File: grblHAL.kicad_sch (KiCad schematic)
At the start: 49 parts, among them J1 Conn_01x03, J2 Conn_02x08_Odd_Even, J3 Conn_01x06, J4 Conn_01x06, J5 Conn_01x04, U1 YAAJ_BluePill_Part_Like_SWD_B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, U10 PC817, U11 PC817, U12 PC817, U13 PC817, U14 LM1117-3.3, U2 TMC2208_SILENTSTEPSTICK, U3 buck2596, U4 PC817, U5 PC817, U6 PC817, U7 PC817, U8 PC817, U9 PC817

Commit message: Schematic Layout Nets Opto 4 TMC Stage 2
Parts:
- added C3, C4: 100uF/35v, Capacitor_THT:CP_Radial_D8.0mm_P3.50mm, symbol Device:C_Polarized_Small
- added J6, J7, J8: Conn_01x04, Connector_PinHeader_2.54mm:PinHeader_1x04_P2.54mm_Vertical, symbol Connector_Generic:Conn_01x04
- added U15, U16, U17: TMC2208, TMC2208_SILENTSTEPSTICK:MODULE_TMC2208_SILENTSTEPSTICK, symbol TMC2208_SILENTSTEPSTICK:TMC2208_SILENTSTEPSTICK
- J2: value Conn_02x08_Odd_Even -> Conn
- J3, J4: footprint Connector_Phoenix_MC_HighVoltage:PhoenixContact_MC_1,5_6-G-5.08_1x06_P5.08mm_Horizontal -> Connector_Phoenix_MSTB:PhoenixContact_MSTBA_2,5_6-G-5,08_1x06_P5.08mm_Horizontal
- U2: value TMC2208_SILENTSTEPSTICK -> TMC2208
- U3: footprint Buck2596:buck2596 -> DC_DC_LM2596_small:DC_DC_LM2596_small
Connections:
- net EN is gone; now on net STEN: JP1.2 (B), U2.JP1_8 (EN)
- net 3V3: now also U15.JP2_7 (VIO), U16.JP2_7 (VIO), U17.JP2_7 (VIO)
- net 5V: now also U1.18 (5V); no longer C1.2, C2.2, JP1.1 (A), R12.1, R13.1, U1.19 (GND), U1.39 (GND), U10.3, U11.3, U12.3, U13.3, U14.1 (GND), U2.JP2_2 (GND), U2.JP2_8 (GND), U3.4 (out-), U4.3, U5.3, U6.3, U7.3, U8.3, U9.3
- net DIRX: now also U17.JP1_1 (DIR)
- net DIRY: now also U16.JP1_1 (DIR)
- net DIRZ: now also U15.JP1_1 (DIR)
- net STEN: now also U15.JP1_8 (EN), U16.JP1_8 (EN), U17.JP1_8 (EN)
- net STEPX: now also U17.JP1_2 (STEP)
- net STEPY: now also U16.JP1_2 (STEP)
- net STEPZ: now also U15.JP1_2 (STEP)
- net VM: now also C3.1, C4.1, U15.JP2_1 (VM), U16.JP2_1 (VM), U17.JP2_1 (VM)
- new net: J6.1 (Pin_1), U15.JP2_3 (OA2)
- new net: J6.2 (Pin_2), U15.JP2_4 (OA1)
- new net: J6.3 (Pin_3), U15.JP2_5 (OB1)
- new net: J6.4 (Pin_4), U15.JP2_6 (OB2)
- new net: J7.1 (Pin_1), U16.JP2_3 (OA2)
- new net: J7.2 (Pin_2), U16.JP2_4 (OA1)
- new net: J7.3 (Pin_3), U16.JP2_5 (OB1)
- new net: J7.4 (Pin_4), U16.JP2_6 (OB2)
- new net: J8.1 (Pin_1), U17.JP2_3 (OA2)
- new net: J8.2 (Pin_2), U17.JP2_4 (OA1)
- new net: J8.3 (Pin_3), U17.JP2_5 (OB1)
- new net: J8.4 (Pin_4), U17.JP2_6 (OB2)
- new net GND: C1.2, C2.2, C3.2, C4.2, JP1.1 (A), R12.1, R13.1, U1.19 (GND), U1.39 (GND), U10.3, U11.3, U12.3, U13.3, U14.1 (GND), U15.JP2_2 (GND), U15.JP2_8 (GND), U16.JP2_2 (GND), U16.JP2_8 (GND), U17.JP2_2 (GND), U17.JP2_8 (GND), U2.JP2_2 (GND), U2.JP2_8 (GND), U3.4 (out-), U4.3, U5.3, U6.3, U7.3, U8.3, U9.3
- new net UART1_PDN2: U15.JP1_4 (PDN/UART1)
- new net UART1_PDN3: U16.JP1_4 (PDN/UART1)
- new net UART1_PDN4: U17.JP1_4 (PDN/UART1)
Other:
- moved on the sheet: C1, C2, D1, D10, D11, D12, D13, D2, D3, D4, D5, D6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

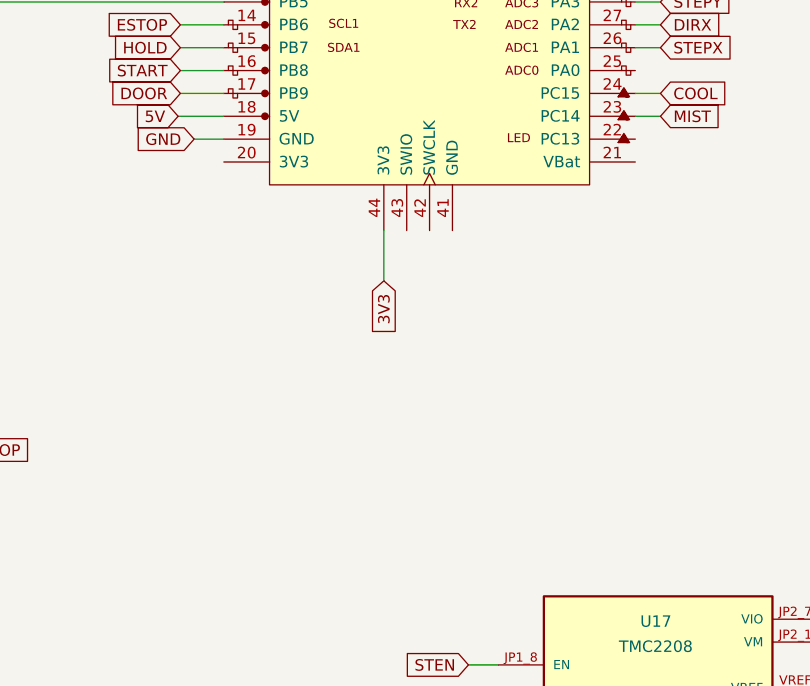
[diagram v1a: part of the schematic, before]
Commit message: Schematic Full Layout Nets Opto Connector 4-TMC Stage 3
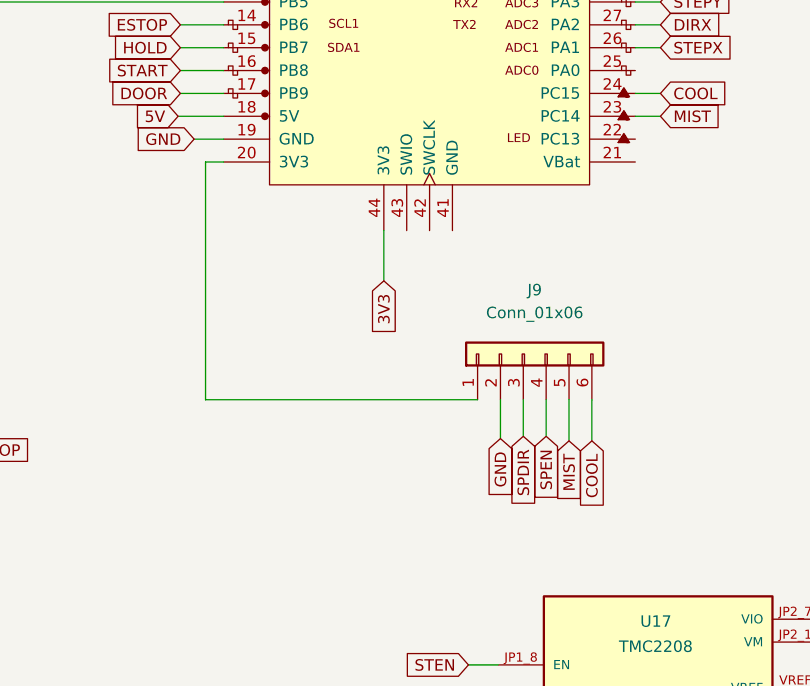
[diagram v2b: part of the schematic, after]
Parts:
- added J9: Conn_01x06, Connector_PinHeader_2.54mm:PinHeader_1x06_P2.54mm_Vertical, symbol Connector_Generic:Conn_01x06
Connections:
- net COOL: now also J9.6 (Pin_6)
- net GND: now also J9.2 (Pin_2)
- net MIST: now also J9.5 (Pin_5)
- net SPDIR: now also J9.3 (Pin_3)
- net SPEN: now also J9.4 (Pin_4)
- net at U1.20 (3V3): now also J9.1 (Pin_1)
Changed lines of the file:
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@@
+    (stroke (width 0) (type default) (color 0 0 0 0))
+  )
+  (wire (pts (xy 95.758 98.552) (xy 125.984 98.552))
     (stroke (width 0) (type default) (color 0 0 0 0))
   )
@@
     (stroke (width 0) (type default) (color 0 0 0 0))
   )
+  (wire (pts (xy 131.064 98.552) (xy 131.064 102.616))
+    (stroke (width 0) (type default) (color 0 0 0 0))
+  )
   (wire (pts (xy 37.846 128.27) (xy 40.64 128.27))
     (stroke (width 0) (type default) (color 0 0 0 0))
   )
+  (wire (pts (xy 133.604 98.552) (xy 133.604 102.616))
+    (stroke (width 0) (type default) (color 0 0 0 0))
+  )
   (wire (pts (xy 30.734 100.33) (xy 32.766 100.33))
     (stroke (width 0) (type default) (color 0 0 0 0))
@@
     (stroke (width 0) (type default) (color 0 0 0 0))
   )
+  (wire (pts (xy 128.524 98.552) (xy 128.524 102.87))
+    (stroke (width 0) (type default) (color 0 0 0 0))
+  )
   (wire (pts (xy 64.516 120.904) (xy 59.69 120.904))
     (stroke (width 0) (type default) (color 0 0 0 0))
@@
     (stroke (width 0) (type default) (color 0 0 0 0))
   )
+  (wire (pts (xy 138.684 98.552) (xy 138.684 103.124))
+    (stroke (width 0) (type default) (color 0 0 0 0))
+  )
+  (wire (pts (xy 97.79 72.136) (xy 95.758 72.136))
+    (stroke (width 0) (type default) (color 0 0 0 0))
+  )
   (wire (pts (xy 131.064 171.704) (xy 138.684 171.704))
     (stroke (width 0) (type default) (color 0 0 0 0))
@@
     (stroke (width 0) (type default) (color 0 0 0 0))
   )
+  (wire (pts (xy 95.758 72.136) (xy 95.758 98.552))
+    (stroke (width 0) (type default) (color 0 0 0 0))
+  )
   (wire (pts (xy 92.964 56.896) (xy 97.79 56.896))
     (stroke (width 0) (type default) (color 0 0 0 0))
@@
   )
   (wire (pts (xy 94.234 31.496) (xy 97.79 31.496))
+    (stroke (width 0) (type default) (color 0 0 0 0))
+  )
+  (wire (pts (xy 136.144 98.552) (xy 136.144 103.124))
     (stroke (width 0) (type default) (color 0 0 0 0))
   )
@@
     )
   )
+  (global_label "SPDIR" (shape input) (at 131.064 102.616 270) (fields_autoplaced)
+    (effects (font (size 1.27 1.27)) (justify right))
+    (property "Intersheet References" "${INTERSHEET_REFS}" (id 0) (at 131.1434 110.6534 90)
+      (effects (font (size 1.27 1.27)) (justify right) hide)
+    )
+  )
   (global_label "VM" (shape input) (at 258.318 64.008 0) (fields_autoplaced)
     (effects (font (size 1.27 1.27)) (justify left))
@@
     )
   )
+  (global_label "GND" (shape input) (at 128.524 102.87 270) (fields_autoplaced)
+    (effects (font (size 1.27 1.27)) (justify right))
+    (property "Intersheet References" "${INTERSHEET_REFS}" (id 0) (at 128.6034 109.1536 90)
+      (effects (font (size 1.27 1.27)) (justify right) hide)
+    )
+  )
   (global_label "SPWM" (shape input) (at 94.234 34.036 180) (fields_autoplaced)
     (effects (font (size 1.27 1.27)) (justify right))
@@
     )
   )
+  (global_label "MIST" (shape input) (at 136.144 103.124 270) (fields_autoplaced)
+    (effects (font (size 1.27 1.27)) (justify right))
+    (property "Intersheet References" "${INTERSHEET_REFS}" (id 0) (at 136.2234 109.7704 90)
+      (effects (font (size 1.27 1.27)) (justify right) hide)
+    )
+  )
   (global_label "STEPA" (shape input) (at 209.804 33.528 180) (fields_autoplaced)
     (effects (font (size 1.27 1.27)) (justify right))
@@
     (property "Intersheet References" "${INTERSHEET_REFS}" (id 0) (at 258.6507 61.5474 0)
       (effects (font (size 1.27 1.27)) (justify left) hide)
+    )
+  )
+  (global_label "COOL" (shape input) (at 138.684 103.124 270) (fields_autoplaced)
+    (effects (font (size 1.27 1.27)) (justify right))
+    (property "Intersheet References" "${INTERSHEET_REFS}" (id 0) (at 138.7634 110.4961 90)
+      (effects (font (size 1.27 1.27)) (justify right) hide)
+    )
+  )
+  (global_label "SPEN" (shape input) (at 133.604 102.616 270) (fields_autoplaced)
+    (effects (font (size 1.27 1.27)) (justify right))
+    (property "Intersheet References" "${INTERSHEET_REFS}" (id 0) (at 133.6834 109.9881 90)
+      (effects (font (size 1.27 1.27)) (justify right) hide)
     )
   )
@@
     (pin "3")
     (pin "4")
+  )
+  (symbol (lib_id "Connector_Generic:Conn_01x06") (at 131.064 93.472 90) (unit 1)
+    (in_bom yes) (on_board yes) (fields_autoplaced)
+    (property "Reference" "J9" (id 0) (at 132.334 86.36 90))
+    (property "Value" "Conn_01x06" (id 1) (at 132.334 88.9 90))
+    (property "Footprint" "Connector_PinHeader_2.54mm:PinHeader_1x06_P2.54mm_Vertical" (id 2) (at 131.064 93.472 0)
+      (effects (font (size 1.27 1.27)) hide)
+    )
+    (property "Datasheet" "~" (id 3) (at 131.064 93.472 0)
+      (effects (font (size 1.27 1.27)) hide)
+    )
+    (pin "1")
+    (pin "2")
+    (pin "3")
+    (pin "4")
+    (pin "5")
+    (pin "6")
   )
   (symbol (lib_id "Connector_Generic:Conn_01x04") (at 264.668 36.068 0) (unit 1)
@@
       (reference "J8") (unit 1) (value "Conn_01x04") (footprint "Connector_PinHeader_2.54mm:PinHeader_1x04_P2.54mm_Vertical")
     )
+    (path "/e41a93a0-713d-4ec5-86b5-71c5a87082fe"
+      (reference "J9") (unit 1) (value "Conn_01x06") (footprint "Connector_PinHeader_2.54mm:PinHeader_1x06_P2.54mm_Vertical")
+    )
     (path "/74aac7d5-7f38-4cd9-8ecb-e6c72de4f237"
